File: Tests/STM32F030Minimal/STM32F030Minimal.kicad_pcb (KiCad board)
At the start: 2 copper layers, 29.2 x 25.5 mm, 15 parts, among them J1 Aux, J2 Left, J3 Right, J4 Prog, U1 STM32F030F4Px, Y1 8MHz

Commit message: Inital commit
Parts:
- moved C7 4.71 mm to (151.7, 73.5)
- moved J2 3.00 mm to (156.8, 87.9)
- moved J3 2.25 mm to (162.0, 90.4)
- moved C2 1.50 mm to (150.9, 70.0)
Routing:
- net VCC: track 39.2 -> 41.6 mm
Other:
- outline, holes or cut-outs redrawn
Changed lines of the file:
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@@
     (thickness 1.6)
     (drawings 18)
-    (tracks 75)
+    (tracks 80)
     (zones 0)
     (modules 15)
@@
     (tags capacitor)
     (attr smd)
-    (fp_text reference C1 (at 0 -1.65) (layer F.SilkS)
+    (fp_text reference C1 (at 2.6875 0) (layer F.SilkS)
       (effects (font (size 1 1) (thickness 0.15)))
     )
@@
   )
   (module Capacitor_SMD:C_0805_2012Metric (layer F.Cu)
-    (at 150.9375 71.5 180)
+    (at 150.9375 70 180)
     (descr "Capacitor SMD 0805 (2012 Metric), square (rectangular) end terminal, IPC_7351 nominal, (Body size source: https://docs.google.com/spreadsheets/d/1BsfQQcO9C6DZCsRaXUlFlo91Tg2WpOkGARC1WS5S8t0/edit?usp=sharing), generated with kicad-footprint-generator")
     (tags capacitor)
     (attr smd)
-    (fp_text reference C2 (at 0 -1.65) (layer F.SilkS)
+    (fp_text reference C2 (at 2.6875 0) (layer F.SilkS)
       (effects (font (size 1 1) (thickness 0.15)))
     )
@@
   )
   (module Capacitor_SMD:C_0805_2012Metric (layer F.Cu)
-    (at 155.3125 76.5 180)
+    (at 151.6875 73.5 180)
     (descr "Capacitor SMD 0805 (2012 Metric), square (rectangular) end terminal, IPC_7351 nominal, (Body size source: https://docs.google.com/spreadsheets/d/1BsfQQcO9C6DZCsRaXUlFlo91Tg2WpOkGARC1WS5S8t0/edit?usp=sharing), generated with kicad-footprint-generator")
     (tags capacitor)
@@
   )
   (module Connector_PinHeader_2.54mm:PinHeader_1x05_P2.54mm_Vertical (layer F.Cu)
-    (at 159.75 87.87 180)
+    (at 156.75 87.87 180)
     (descr "Through hole straight pin header, 1x05, 2.54mm pitch, single row")
     (tags "Through hole pin header THT 1x05 2.54mm single row")
@@
   )
   (module Connector_PinHeader_2.54mm:PinHeader_1x06_P2.54mm_Vertical (layer F.Cu)
-    (at 164.25 90.37 180)
+    (at 162 90.37 180)
     (descr "Through hole straight pin header, 1x06, 2.54mm pitch, single row")
     (tags "Through hole pin header THT 1x06 2.54mm single row")
@@
   (gr_line (start 146.25 53) (end 173 53) (layer Edge.Cuts) (width 0.05))
   (gr_line (start 145 77.25) (end 145 54.25) (layer Edge.Cuts) (width 0.05))
-  (gr_line (start 157.25 78.5) (end 146.25 78.5) (layer Edge.Cuts) (width 0.05))
+  (gr_line (start 152.75 78.5) (end 146.25 78.5) (layer Edge.Cuts) (width 0.05))
   (segment (start 155.750001 68.550001) (end 154.75 67.55) (width 0.25) (layer F.Cu) (net 2))
   (segment (start 158.875001 68.550001) (end 155.750001 68.550001) (width 0.25) (layer F.Cu) (net 2))
@@
   (segment (start 155.549999 69.200001) (end 154.75 70) (width 0.25) (layer F.Cu) (net 3))
   (segment (start 158.875001 69.200001) (end 155.549999 69.200001) (width 0.25) (layer F.Cu) (net 3))
-  (segment (start 152.125 71.25) (end 151.875 71.5) (width 0.25) (layer F.Cu) (net 3))
-  (segment (start 154.75 71.25) (end 152.125 71.25) (width 0.25) (layer F.Cu) (net 3))
-  (segment (start 147.5 67.125) (end 151.875 71.5) (width 0.25) (layer F.Cu) (net 3))
-  (segment (start 147.5 63.83) (end 147.5 67.125) (width 0.25) (layer F.Cu) (net 3))
+  (segment (start 153.125 71.25) (end 151.875 70) (width 0.25) (layer F.Cu) (net 3))
+  (segment (start 154.75 71.25) (end 153.125 71.25) (width 0.25) (layer F.Cu) (net 3))
+  (segment (start 147.85 63.83) (end 146.75 63.83) (width 0.25) (layer F.Cu) (net 3))
+  (segment (start 150.81251 66.79251) (end 147.85 63.83) (width 0.25) (layer F.Cu) (net 3))
+  (segment (start 151.875 70) (end 150.81251 68.93751) (width 0.25) (layer F.Cu) (net 3))
+  (segment (start 150.81251 68.93751) (end 150.81251 66.79251) (width 0.25) (layer F.Cu) (net 3))
   (segment (start 157.8125 64.5) (end 158.0625 64.25) (width 0.25) (layer F.Cu) (net 4))
   (segment (start 155.75 64.5) (end 157.8125 64.5) (width 0.25) (layer F.Cu) (net 4))
@@
   (segment (start 157.989999 70.500001) (end 156.806237 71.683763) (width 0.25) (layer F.Cu) (net 5))
   (segment (start 158.875001 70.500001) (end 157.989999 70.500001) (width 0.25) (layer F.Cu) (net 5))
-  (segment (start 155.693763 75.943763) (end 156.25 76.5) (width 0.25) (layer F.Cu) (net 5))
-  (segment (start 155.693763 74.056237) (end 155.693763 75.943763) (width 0.25) (layer F.Cu) (net 5))
-  (segment (start 156.25 73.5) (end 155.693763 74.056237) (width 0.25) (layer F.Cu) (net 5))
-  (via (at 157.25 76) (size 0.8) (drill 0.4) (layers F.Cu B.Cu) (net 5))
-  (segment (start 156.25 76.5) (end 156.75 76.5) (width 0.25) (layer F.Cu) (net 5))
-  (segment (start 156.75 76.5) (end 157.25 76) (width 0.25) (layer F.Cu) (net 5))
-  (segment (start 161.09 72.16) (end 161.09 68.41) (width 0.25) (layer B.Cu) (net 5))
-  (segment (start 157.25 76) (end 161.09 72.16) (width 0.25) (layer B.Cu) (net 5))
   (segment (start 161.09 60.5) (end 165.045 64.455) (width 0.25) (layer B.Cu) (net 5))
   (segment (start 161.09 68.41) (end 165.045 64.455) (width 0.25) (layer B.Cu) (net 5))
   (segment (start 165.045 64.455) (end 166.5 65.91) (width 0.25) (layer B.Cu) (net 5))
+  (segment (start 155.693763 74.056237) (end 156.25 73.5) (width 0.25) (layer F.Cu) (net 5))
+  (segment (start 155.22499 74.52501) (end 155.693763 74.056237) (width 0.25) (layer F.Cu) (net 5))
+  (segment (start 153.65001 74.52501) (end 155.22499 74.52501) (width 0.25) (layer F.Cu) (net 5))
+  (via (at 153 75) (size 0.8) (drill 0.4) (layers F.Cu B.Cu) (net 5))
+  (segment (start 161.09 68.41) (end 159.59 68.41) (width 0.25) (layer B.Cu) (net 5))
+  (segment (start 159.59 68.41) (end 153 75) (width 0.25) (layer B.Cu) (net 5))
+  (segment (start 153.399999 74.600001) (end 153.399999 74.350001) (width 0.25) (layer F.Cu) (net 5))
+  (segment (start 153.399999 74.350001) (end 153.4375 74.3125) (width 0.25) (layer F.Cu) (net 5))
+  (segment (start 153 75) (end 153.399999 74.600001) (width 0.25) (layer F.Cu) (net 5))
+  (segment (start 152.625 73.5) (end 153.4375 74.3125) (width 0.25) (layer F.Cu) (net 5))
+  (segment (start 153.4375 74.3125) (end 153.65001 74.52501) (width 0.25) (layer F.Cu) (net 5))
   (segment (start 148.702081 58.75) (end 147.5 58.75) (width 0.25) (layer F.Cu) (net 6))
   (segment (start 148.985002 58.75) (end 148.702081 58.75) (width 0.25) (layer F.Cu) (net 6))

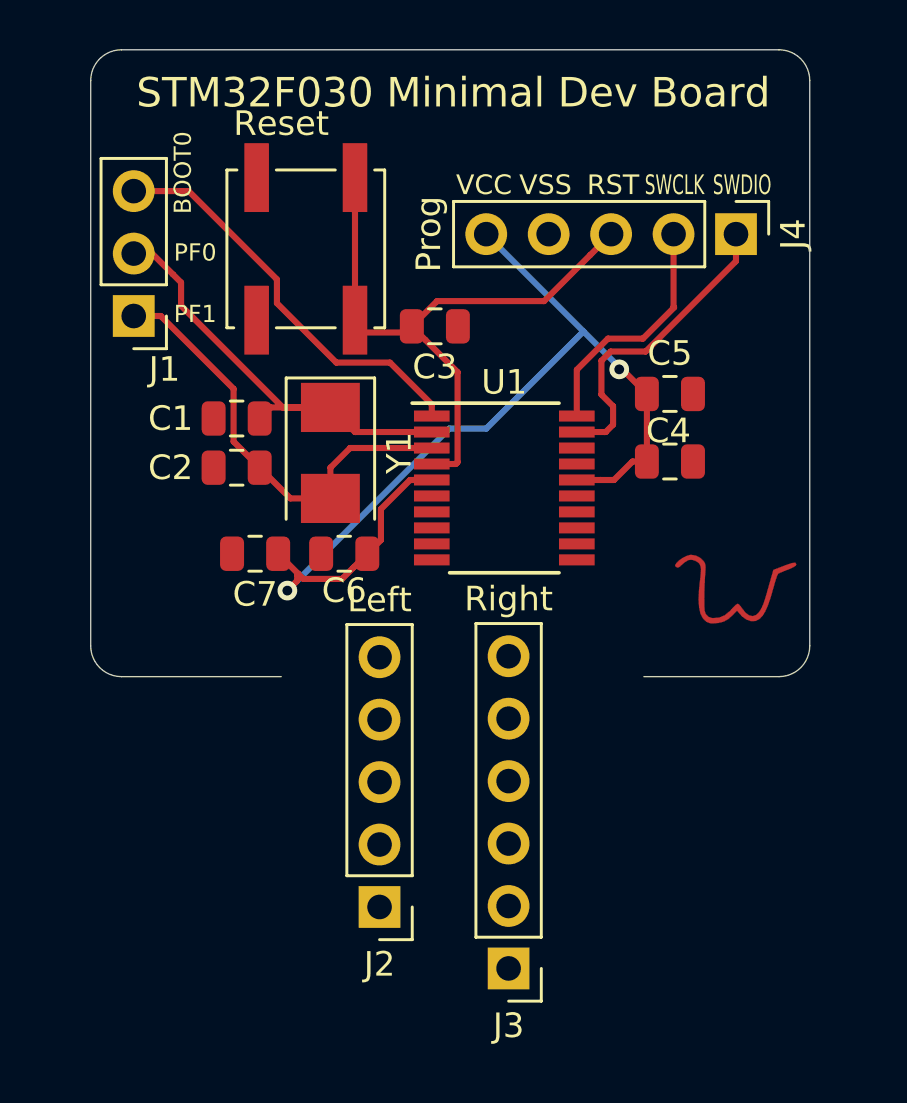
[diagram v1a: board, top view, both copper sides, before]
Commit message: Ordered V1 of two different minimal dev boards
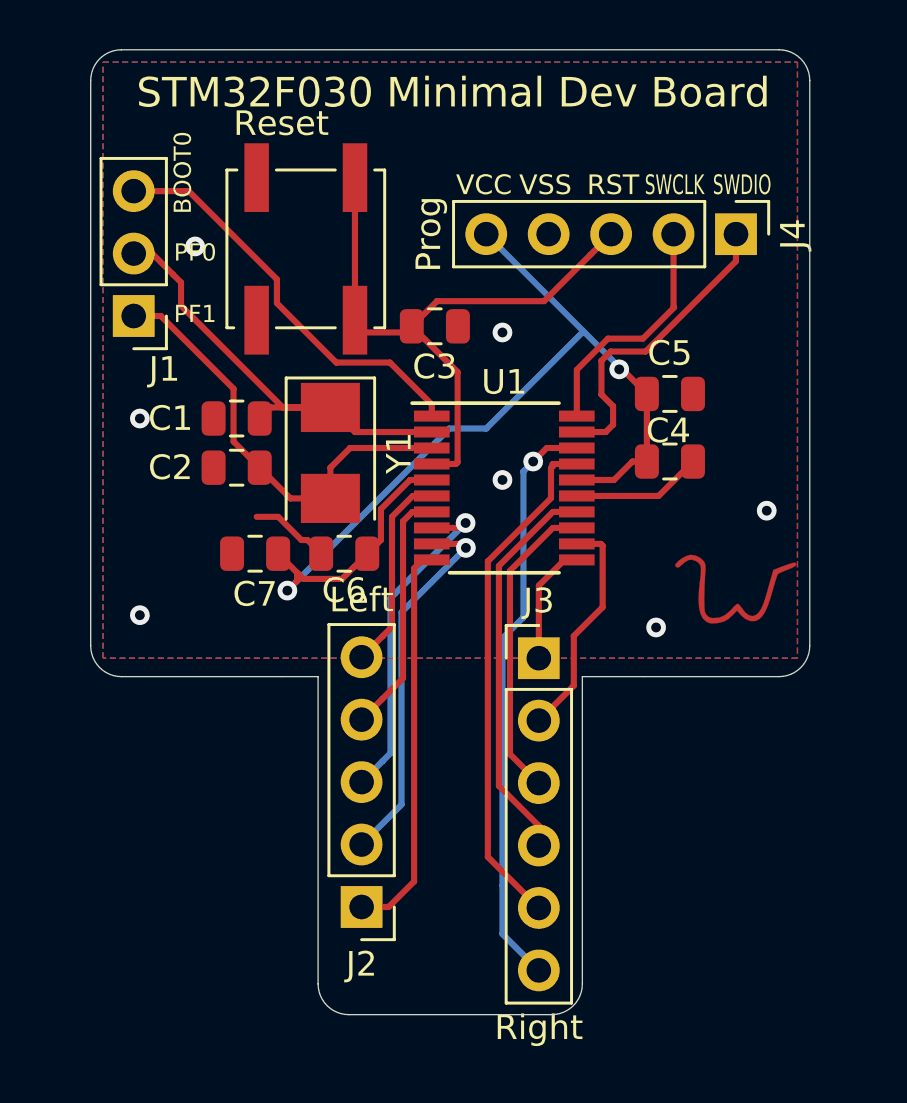
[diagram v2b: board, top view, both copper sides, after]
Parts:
- moved J3 12.7 mm to (163.2, 77.8), turned to 0 degrees
- moved J2 0.73 mm to (156.0, 87.9)
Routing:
- net PA10: track 0.00 -> 23.8 mm, vias 0 -> 1
- net PA9: track 0.00 -> 21.6 mm
- net PA4: track 0.00 -> 16.2 mm
- net PB1: track 0.00 -> 16.1 mm
- net PA3: track 0.00 -> 15.3 mm, vias 0 -> 1
- net PA2: track 0.00 -> 13.7 mm, vias 0 -> 1
- net PA7: track 0.00 -> 12.6 mm
- net PA1: track 0.00 -> 10.1 mm
- net PA6: track 0.00 -> 9.27 mm
- net VSS: track 0.00 -> 8.55 mm, vias 0 -> 7
- net PA0: track 0.00 -> 8.20 mm
- net PA5: track 0.00 -> 4.93 mm
- added copper zone on B.Cu, net VSS
- added copper zone on F.Cu, net VSS
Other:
- board size 29.2 x 25.5 mm -> 29.2 x 39.2 mm
- board text added: "V1"
